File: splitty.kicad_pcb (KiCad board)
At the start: 2 copper layers, 133.4 x 100.3 mm, 97 parts, among them J1 USB_B_Micro, J2 USB_B_Micro, J3 Conn_01x06, J4 Conn_01x05, SW0 SW_Push, SW1 SW_Push, SW10 SW_Push, SW11 SW_Push, SW12 SW_Push, SW13 SW_Push, SW14 SW_Push, SW16 SW_Push, SW17 SW_Push, SW18 SW_Push, SW19 SW_Push, SW2 SW_Push, SW20 SW_Push, SW21 SW_Push, SW24 SW_Push, SW25 SW_Push, SW26 SW_Push, SW27 SW_Push, SW28 SW_Push, SW29 SW_Push, SW3 SW_Push, SW30 SW_Push, SW34 SW_Push, SW35 SW_Push, SW36 SW_Push, SW37 SW_Push, SW38 SW_Push, SW4 SW_Push, SW40 SW_Push, SW5 SW_Push, SW6 SW_Push, SW8 SW_Push, SW9 SW_Push, U1 ATmega32U4-AU, U2 USBLC6-2, U3 USBLC6-2, Y1 16M

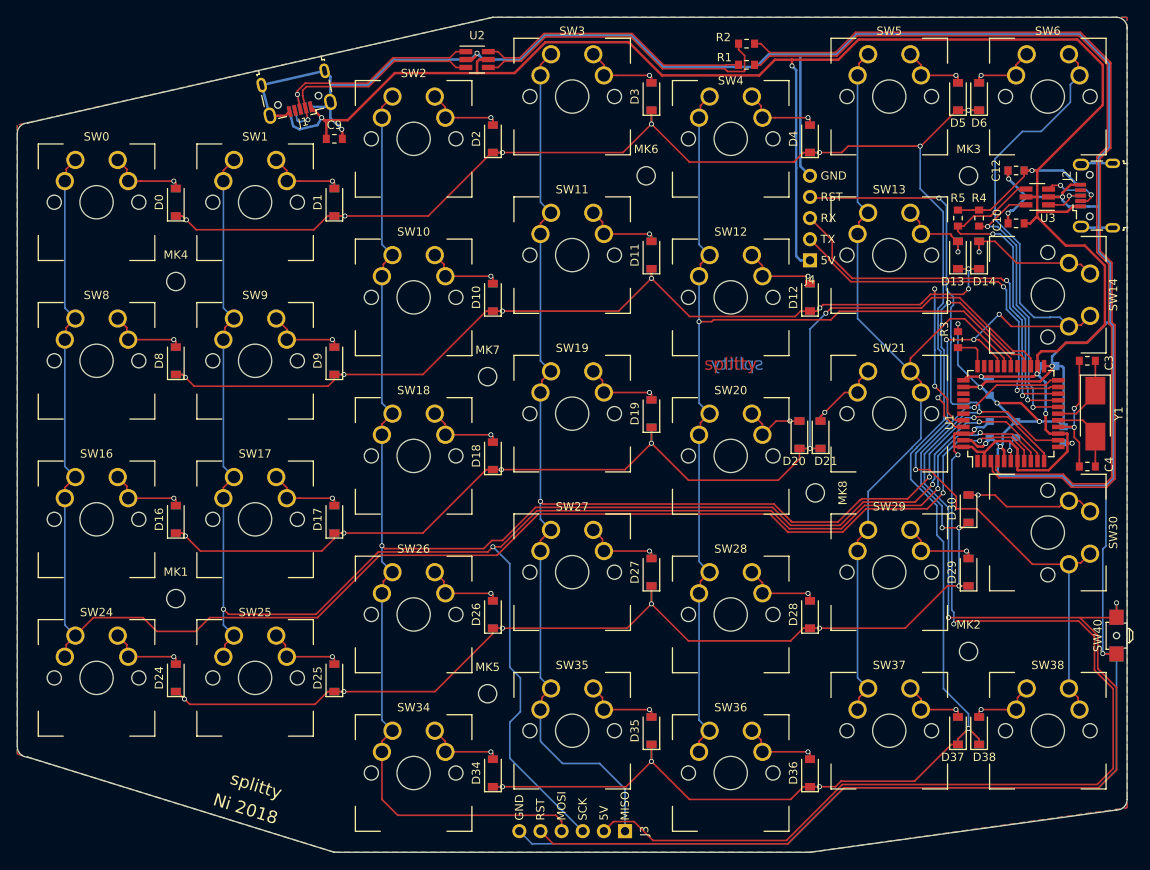
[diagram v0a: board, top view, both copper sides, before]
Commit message: Update to Kicad 5
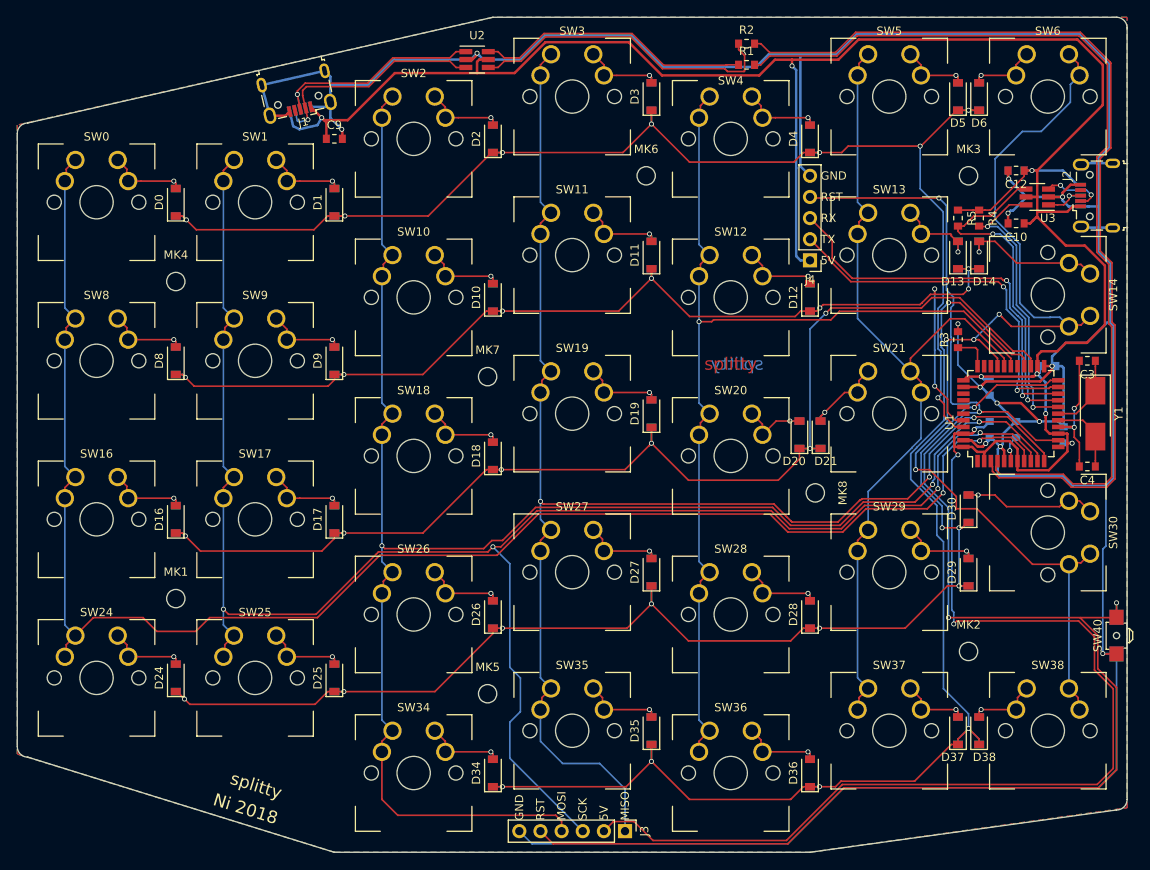
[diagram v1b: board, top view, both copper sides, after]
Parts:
- C1, C10, C11, C12, C3, C4, C5, C6, C7, C8, C9: footprint Capacitor_SMD:C_0603_1608Metric_Pad0.84x1.00mm_HandSolder -> splitty:C_0603_1608Metric_Pad0.84x1.00mm_HandSolder
- R1, R2, R3, R4, R5: footprint Resistor_SMD:R_0603_1608Metric_Pad0.84x1.00mm_HandSolder -> splitty:R_0603_1608Metric_Pad0.84x1.00mm_HandSolder
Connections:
- U1 pad 1: (no net) -> Net-(U1-Pad1)
- U1 pad 12: (no net) -> Net-(U1-Pad12)
- U1 pad 27: (no net) -> Net-(U1-Pad27)
- U1 pad 31: (no net) -> Net-(U1-Pad31)
- U1 pad 32: (no net) -> Net-(U1-Pad32)
- U1 pad 36: (no net) -> Net-(U1-Pad36)
- U1 pad 37: (no net) -> Net-(U1-Pad37)
- U1 pad 38: (no net) -> Net-(U1-Pad38)
- U1 pad 39: (no net) -> Net-(U1-Pad39)
